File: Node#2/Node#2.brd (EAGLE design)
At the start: 60.5 x 120 mm, 94 parts, among them IC1 TSL25911FN, J1 68712414522, Q1 BC847ALT1SMD, Q2 SI1308EDL-T1-GE3, U2 RV8564C3, U4 TPS63001DRCT

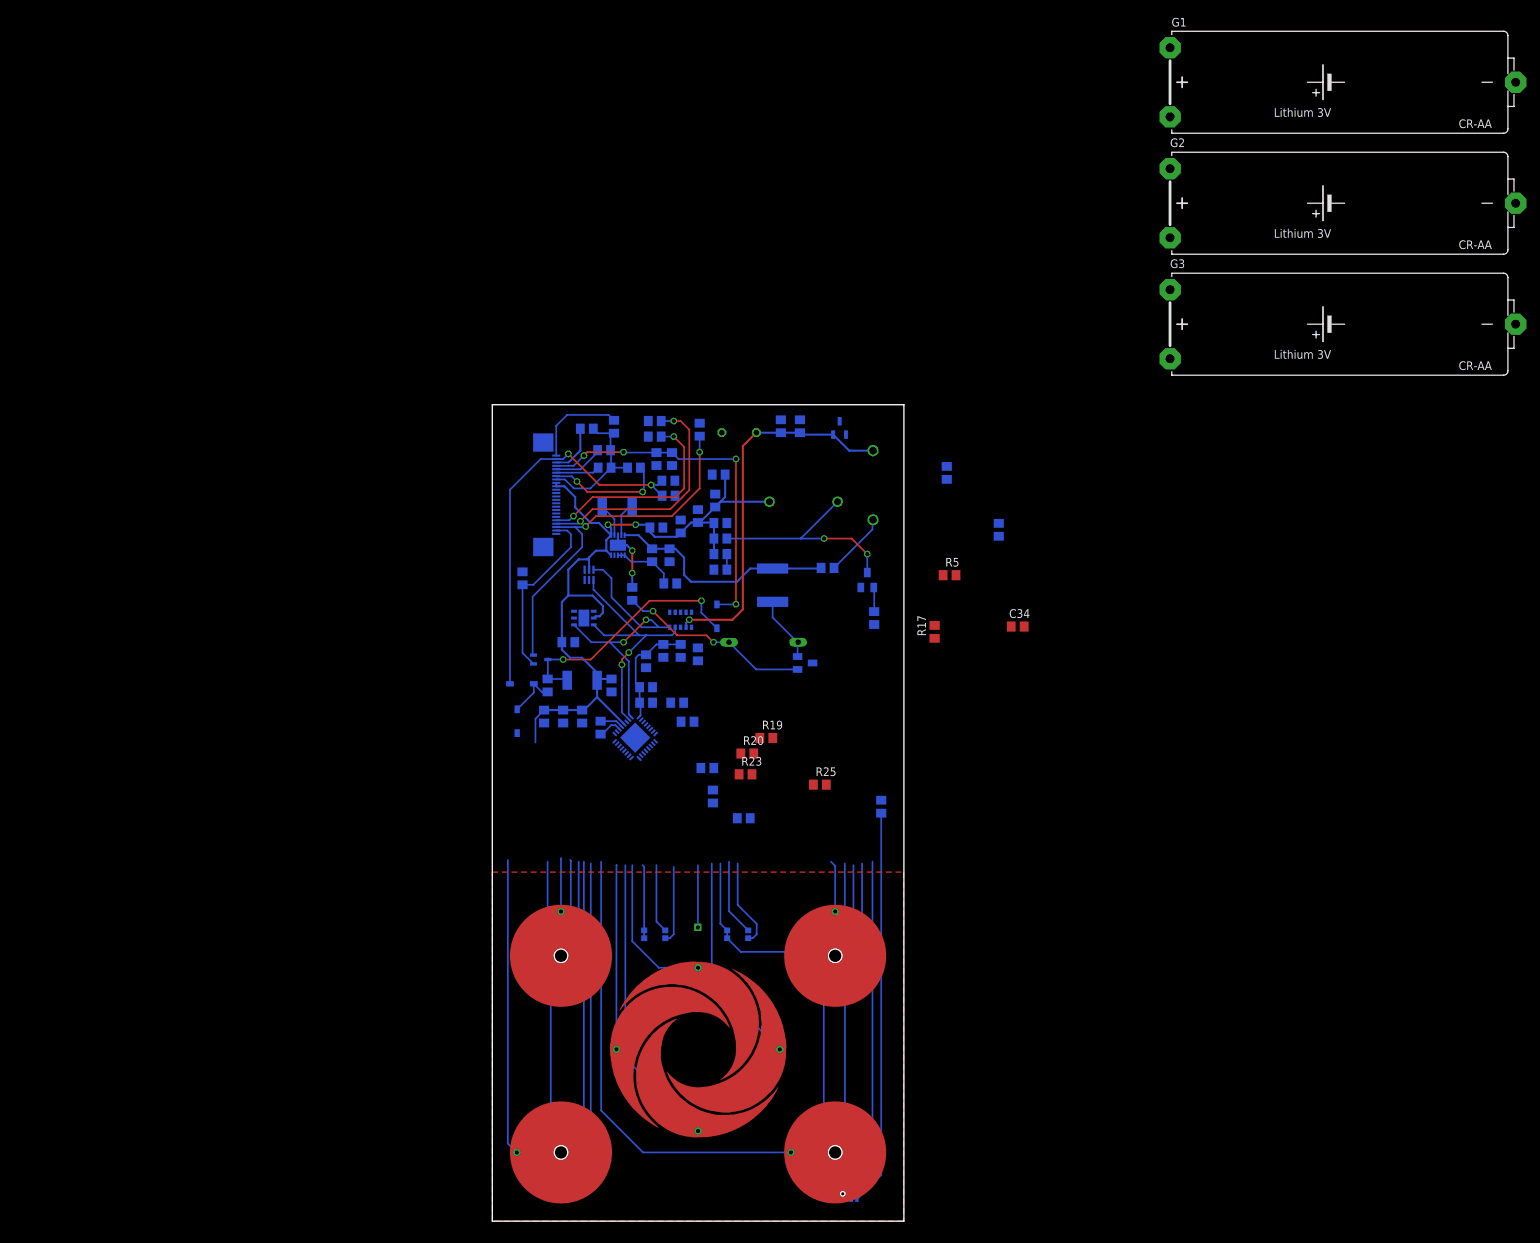
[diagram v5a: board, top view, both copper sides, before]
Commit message: Layout von Node#2 fertiggestellt
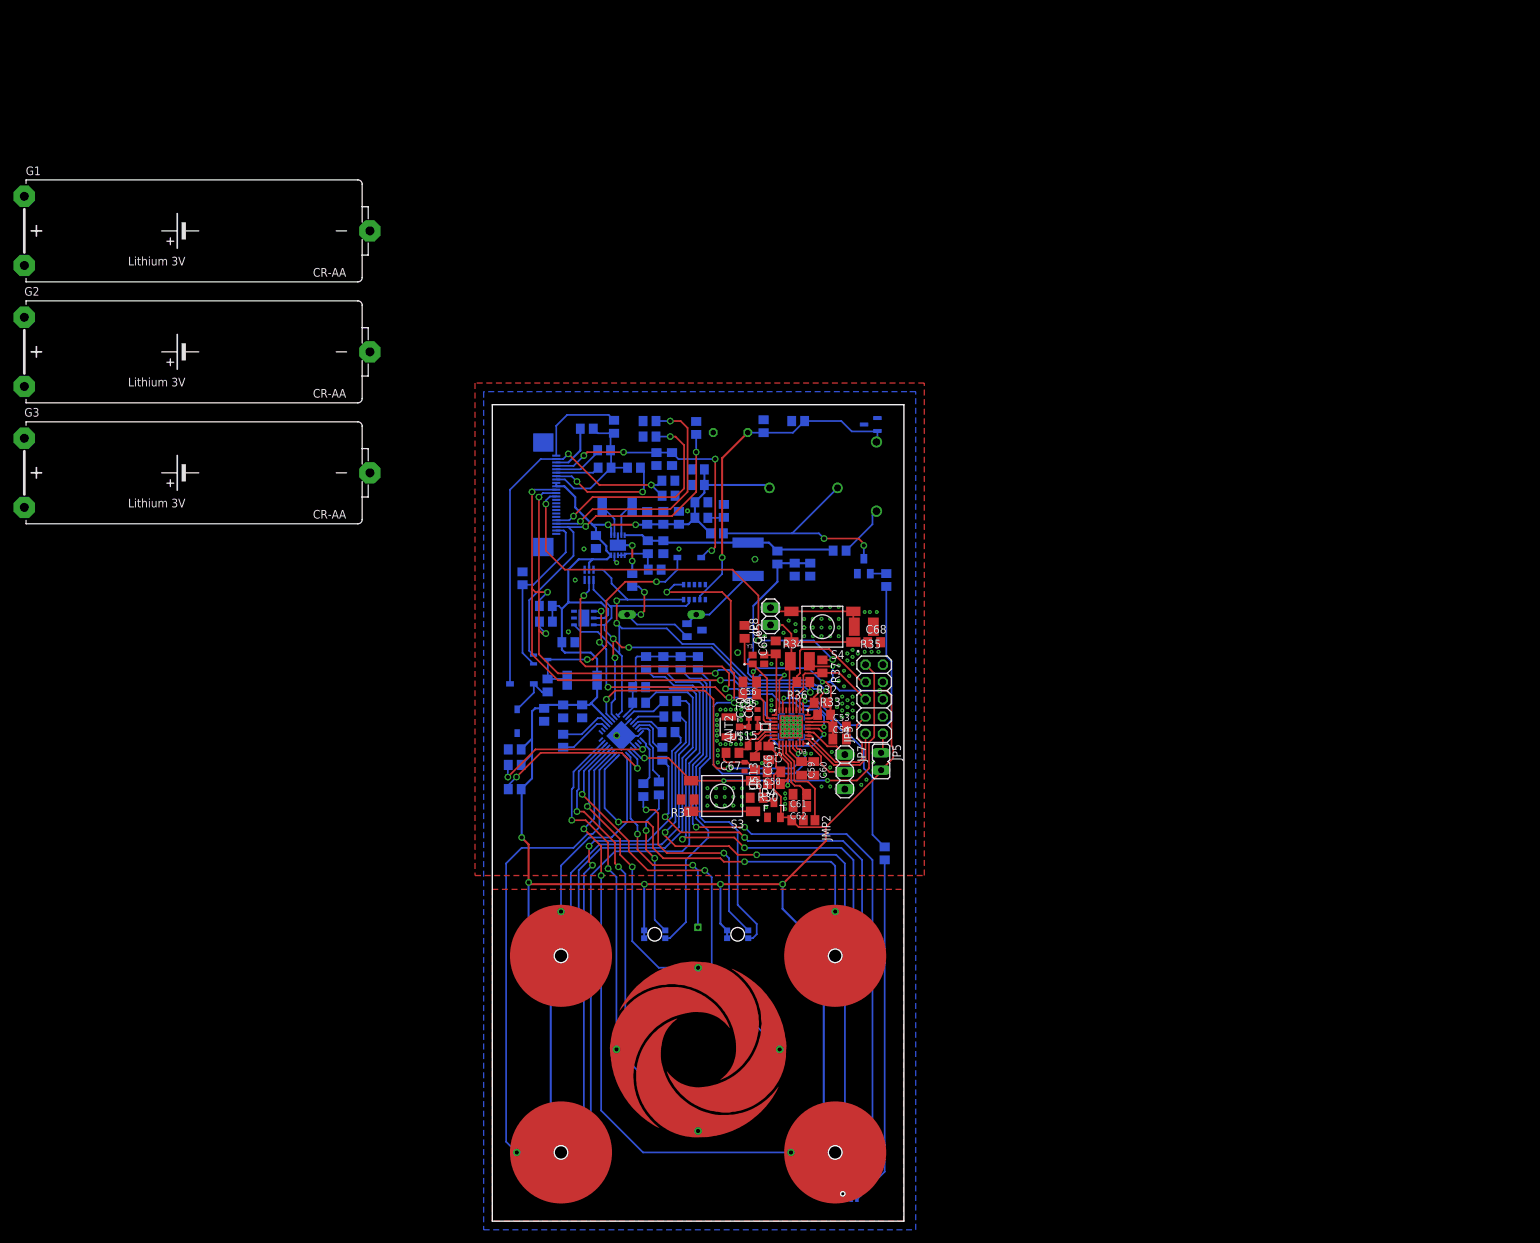
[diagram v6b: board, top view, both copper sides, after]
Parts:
- added ANT2: CONUFL001-SMD, BlueHome:CONUFL001-SMD
- added C53, C54, C55, C56, C57, C58, C59, C60, C61, C62: (no value), rcl:C0805K
- added C63, C64, C65, C66, C67, C68: (no value), rcl:C0805
- added C69, C70: (no value), rcl:C0402
- added D4: BAS40-06, diode:SOT23
- added JMP2: 0R-JUMPA, jump-0r-smd:A0R-JMP
- added JP3: (no value), pinhead:2X05
- added JP5: (no value), jumper:JP1
- added JP7: (no value), pinhead:1X03
- added JP8: (no value), pinhead:1X02
- added R30, R31, R32, R33, R36, R37: (no value), rcl:R0805
- added R34, R35: (no value), rcl:R1210
- added S3, S4: FSM4JSMAATR, BlueHome:SW_FSM4JSMAATR
- added U$13, U$15: L0402, BlueHome:R0402
- added U$14: BALF-NRG-01D3, BlueHome:FLIPCHIP
- added U3: BLUENRG-232, BlueHome:QFN50P500X500X100-33T345N
- added Y3: ECS-160-12-36-AGN-TR, BlueHome:XTAL_ECS-160-12-36-AGN-TR
- added Y4: NX2012SA-32.768K-STD-MUB-1, BlueHome:XTAL_NX2012SA-32.768K-STD-MUB-1
- moved G1 169.8 mm to (-43.4, 145.6)
- moved G2 169.8 mm to (-43.4, 127.8)
- moved G3 169.8 mm to (-43.4, 110.0)
- moved R8 67.9 mm to (7.89, 88.1), turned to 180 degrees
- moved R3 62.1 mm to (7.87, 90.4), turned to 180 degrees
- moved C17 33.9 mm to (3.30, 63.5)
- moved C34 31.6 mm to (46.7, 95.8), flipped to the bottom, turned to 270 degrees
- moved C14 29.9 mm to (3.30, 69.3), turned to 0 degrees
- moved C16 28.3 mm to (3.30, 67.1)
- moved R25 26.0 mm to (22.2, 63.4), flipped to the bottom, turned to 270 degrees
- moved R5 25.4 mm to (41.9, 97.5), flipped to the bottom, turned to 90 degrees
- moved R17 22.5 mm to (44.5, 95.8), flipped to the bottom
- moved C24 21.2 mm to (15.2, 99.8)
- moved !!!FDN304PZ!!! 17.0 mm to (29.7, 86.9)
- moved D1 15.5 mm to (24.9, 89.2)
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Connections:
- removed net MOSI: R3.1
- removed net RESET: U$2.29
- removed net SCLK: R8.1
- new net DIO14: C68.1, JP8.1, R34.1, S4.1, S4.2, U3.13
- new net JTCK: JP3.4, U3.2
- new net JTMS: JP3.2, U3.1
- new net N$48: C59.1, C60.1, U3.28
- new net N$49: C61.1, C62.1, JMP2.2, U3.26
- new net N$50: R31.1, S3.1, S3.2
- new net N$51: C64.1, U3.17, Y3.3
- new net N$52: C65.2, U3.18, Y3.1
- new net N$53: C66.2, C67.2, U$13.1
- new net N$54: C66.1, U3.23, Y4.2
- new net N$55: C67.1, U3.22, Y4.1
- new net N$56: C69.1, U$14.A1, U$15.1
- new net N$57: ANT2.1, C70.1, U$15.2
- new net N$58: JP3.1, JP5.1
- new net N$59: JP8.2, R35.2, S4.3, S4.4
- new net N$60: U$14.B1, U3.20
- new net N$61: U$14.B2, U3.21
- new net RESETN: C63.2, D4.3, JP3.10, R30.1, S3.3, S3.4, U$2.29, U3.25
- new net RXD: JP7.2, U3.32
- new net SMPSFILT2: JMP2.1, U3.27
- new net TDI: JP3.8, R36.2, U3.12
- new net TDO: JP3.6, R37.2, U3.11
- new net TXD: JP7.1, U3.3
- net +3V3: now also C53.1, C54.1, C55.1, C56.1, C57.1, C58.1, D4.2, JMP2.3, JP5.2, R30.2, R32.2, R33.2, R34.2, U3.19, U3.24, U3.6
- net ADC1: now also U3.15
- net ADC2: now also U3.16
- net DIO0: now also R36.1, R8.1
- net DIO1: now also R37.1
- net DIO12: now also U3.30
- net DIO13: now also U3.29
- net DIO2: now also R3.1, U3.10
- net DIO3: now also U3.9
- net DIO6: now also U3.5
- net DIO7: now also U3.4
- net GND: now also ANT2.2, ANT2.3, C53.2, C54.2, C55.2, C56.2, C57.2, C58.2, C59.2, C60.2, C61.2, C62.2, C63.1, C64.2, C65.1, C68.2, C69.2, C70.2, JP3.3, JP3.5, JP3.9, JP7.3, R31.2, R35.1, U$13.2, U$14.A2, U3.31, U3.33, Y3.2, Y3.4
- net SCL: now also R32.1, U3.8
- net SDA: now also R33.1, U3.7
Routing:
- net +3V3: track 236.5 -> 400.9 mm, vias 2 -> 11
- net DIO2: track 0.00 -> 77.4 mm, vias 0 -> 4
- net DIO0: track 0.00 -> 73.4 mm, vias 0 -> 4
- net RESETN: track 0.00 -> 72.6 mm, vias 0 -> 4
- net DIO1: track 0.00 -> 63.4 mm, vias 0 -> 3
- net DIO12: track 0.00 -> 58.2 mm, vias 0 -> 3
- net DIO6: track 0.00 -> 57.7 mm, vias 0 -> 3
- net N$25: track 14.6 -> 72.1 mm, vias 0 -> 2
- net N$27: track 45.8 -> 102.5 mm, vias 0 -> 2
- net DIO7: track 0.00 -> 54.3 mm, vias 0 -> 5
- net N$26: track 13.1 -> 60.8 mm, vias 0 -> 2
- net N$7: track 44.7 -> 91.6 mm
- net N$29: track 7.79 -> 54.5 mm, vias 0 -> 2
- net DIO13: track 0.00 -> 46.1 mm, vias 0 -> 3
- net N$4: track 15.3 -> 59.7 mm
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- added copper zone on layer 1, net GND
- added copper zone on layer 16, net GND

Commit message: Initial V2
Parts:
- removed ANT2: CONUFL001-SMD, BlueHome:CONUFL001-SMD
- removed C53, C54, C55, C56, C57, C58, C59, C60, C61, C62: (no value), rcl:C0805K
- removed C63, C64, C65, C66, C67, C68: (no value), rcl:C0805
- removed C69, C70: (no value), rcl:C0402
- removed D4: BAS40-06, diode:SOT23
- removed JMP2: 0R-JUMPA, jump-0r-smd:A0R-JMP
- removed JP3: (no value), pinhead:2X05
- removed JP5: (no value), jumper:JP1
- removed JP7: (no value), pinhead:1X03
- removed JP8: (no value), pinhead:1X02
- removed R30, R31, R32, R33, R36, R37: (no value), rcl:R0805
- removed R34, R35: (no value), rcl:R1210
- removed S3, S4: FSM4JSMAATR, BlueHome:SW_FSM4JSMAATR
- removed U$13, U$15: L0402, BlueHome:R0402
- removed U$14: BALF-NRG-01D3, BlueHome:FLIPCHIP
- removed U3: BLUENRG-232, BlueHome:QFN50P500X500X100-33T345N
- removed Y3: ECS-160-12-36-AGN-TR, BlueHome:XTAL_ECS-160-12-36-AGN-TR
- removed Y4: NX2012SA-32.768K-STD-MUB-1, BlueHome:XTAL_NX2012SA-32.768K-STD-MUB-1
- R16: value 10k -> 0k
- moved LS1 86.6 mm to (50.0, 21.3), turned to 180 degrees
- moved C34 81.6 mm to (128.3, 93.7)
- moved C10 81.6 mm to (106.7, 97.0)
- moved C13 81.6 mm to (94.7, 72.9)
- moved C19 81.6 mm to (99.4, 114.7)
- moved C22 81.6 mm to (95.4, 114.4)
- moved C24 81.6 mm to (96.8, 97.8)
- moved C26 81.6 mm to (89.7, 76.7)
- moved C27 81.6 mm to (108.0, 110.0)
- moved C29 81.6 mm to (107.4, 106.8)
- moved C30 81.6 mm to (105.7, 110.0)
- moved C31 81.6 mm to (104.3, 101.3)
- moved C4 81.6 mm to (111.8, 108.5)
- moved C5 81.6 mm to (106.7, 101.3)
- moved C7 81.6 mm to (126.5, 115.6)
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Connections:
- removed net CS: R1.1, R18.2
- removed net DIO14: C68.1, JP8.1, R34.1, S4.1, S4.2, U3.13
- removed net JTCK: JP3.4, U3.2
- removed net JTMS: JP3.2, U3.1
- removed net N$48: C59.1, C60.1, U3.28
- removed net N$49: C61.1, C62.1, JMP2.2, U3.26
- removed net N$50: R31.1, S3.1, S3.2
- removed net N$51: C64.1, U3.17, Y3.3
- removed net N$52: C65.2, U3.18, Y3.1
- removed net N$53: C66.2, C67.2, U$13.1
- removed net N$54: C66.1, U3.23, Y4.2
- removed net N$55: C67.1, U3.22, Y4.1
- removed net N$56: C69.1, U$14.A1, U$15.1
- removed net N$57: ANT2.1, C70.1, U$15.2
- removed net N$58: JP3.1, JP5.1
- removed net N$59: JP8.2, R35.2, S4.3, S4.4
- removed net N$60: U$14.B1, U3.20
- removed net N$61: U$14.B2, U3.21
- removed net RXD: JP7.2, U3.32
- removed net SMPSFILT2: JMP2.1, U3.27
- removed net TDI: JP3.8, R36.2, U3.12
- removed net TDO: JP3.6, R37.2, U3.11
- removed net TXD: JP7.1, U3.3
- net +3V3: no longer C53.1, C54.1, C55.1, C56.1, C57.1, C58.1, D4.2, JMP2.3, JP5.2, R30.2, R32.2, R33.2, R34.2, U3.19, U3.24, U3.6
- net ADC1: no longer U3.15
- net ADC2: no longer U3.16
- net DIO0: no longer R36.1
- net DIO1: now also R1.1, R18.2; no longer R37.1
- net DIO12: no longer U3.30
- net DIO13: no longer U3.29
- net DIO2: no longer U3.10
- net DIO3: no longer U3.9
- net DIO6: no longer U3.5
- net DIO7: no longer U3.4
- net GND: no longer ANT2.2, ANT2.3, C53.2, C54.2, C55.2, C56.2, C57.2, C58.2, C59.2, C60.2, C61.2, C62.2, C63.1, C64.2, C65.1, C68.2, C69.2, C70.2, JP3.3, JP3.5, JP3.9, JP7.3, R31.2, R35.1, U$13.2, U$14.A2, U3.31, U3.33, Y3.2, Y3.4
- net RESETN: no longer C63.2, D4.3, JP3.10, R30.1, S3.3, S3.4, U3.25
- net SCL: no longer R32.1, U3.8
- net SDA: no longer R33.1, U3.7
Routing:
- net +3V3: track 400.9 -> 0.00 mm, vias 11 -> 0
- net N$27: track 102.5 -> 0.00 mm, vias 2 -> 0
- net N$7: track 91.6 -> 0.00 mm
- net N$32: track 86.0 -> 0.00 mm, vias 2 -> 0
- net N$30: track 84.0 -> 0.00 mm, vias 2 -> 0
- net SDA: track 83.0 -> 0.00 mm, vias 3 -> 0
- net DIO2: track 77.4 -> 0.00 mm, vias 4 -> 0
- net SCL: track 75.2 -> 0.00 mm, vias 4 -> 0
- net DIO0: track 73.4 -> 0.00 mm, vias 4 -> 0
- net N$13: track 73.3 -> 0.00 mm, vias 2 -> 0
- net RESETN: track 72.6 -> 0.00 mm, vias 4 -> 0
- net N$25: track 72.1 -> 0.00 mm, vias 2 -> 0
- net N$31: track 70.8 -> 0.00 mm
- net SEG3: track 66.6 -> 0.00 mm, vias 2 -> 0
- net DIO1: track 63.4 -> 0.00 mm, vias 3 -> 0
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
